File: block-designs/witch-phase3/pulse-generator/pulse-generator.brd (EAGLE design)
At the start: 159.8 x 99.1 mm, 104 parts, among them IC1 74LVC1G17DBV, IC10 74LVC1G08DBV, IC11 74LVC1G08DBV, IC12 741G175, IC13 741G175, IC14 741G175, IC15 741G175, IC16 741G175, IC17 74LVC1G04DBV, IC18 74LVC1G04DBV, IC19 74LVC1G08DBV, IC2 74LVC1G17DBV, IC20 74LVC1G04DBV, IC21 74LVC1G08DBV, IC22 741G175, IC23 74LVC1G08DBV, IC24 74LVC1G04DBV, IC3 74LVC1G17DBV, IC4 NE555D, IC5 741G175, IC6 74LVC1G04DBV, IC7 74LVC1G04DBV, IC8 741G175, IC9 741G175, J1 POWER_JACKPTH, Q1 MMBT2222A, Q2 MMBT2222A, Q3 MMBT2222A, Q4 MMBT2222A, Q5 MMBT2222A, Q6 MMBT2907ALT1SMD, Q7 MMBT2222A, Q8 MMBT2222A, Q9 MMBT2222A

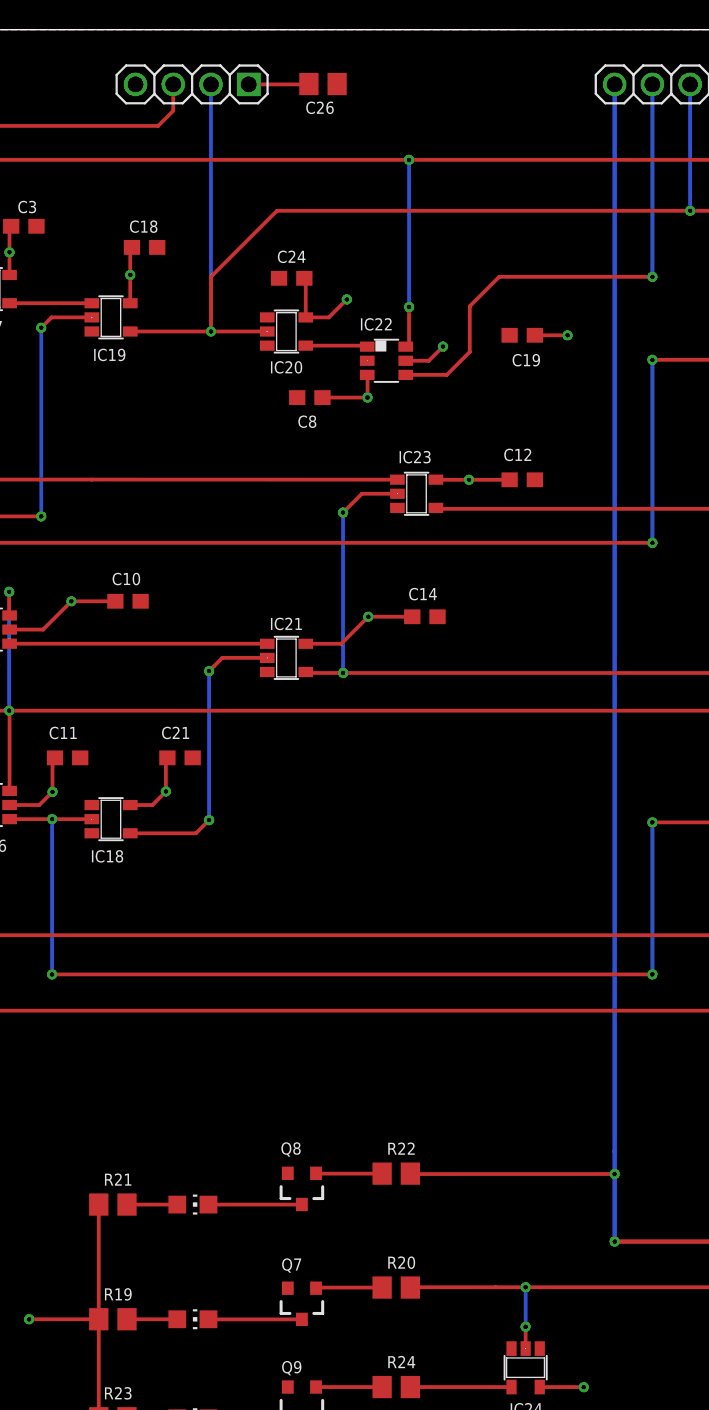
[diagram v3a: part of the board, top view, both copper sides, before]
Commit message: tweak position of function leds
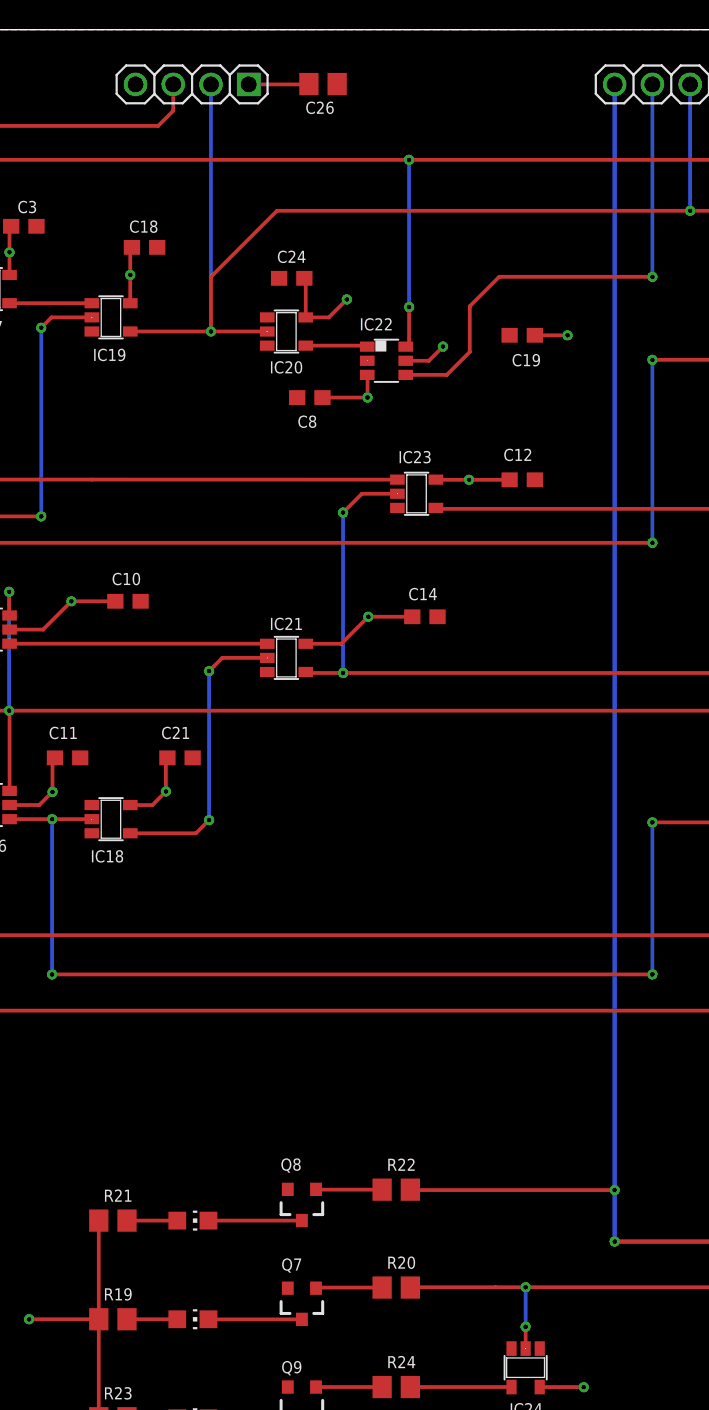
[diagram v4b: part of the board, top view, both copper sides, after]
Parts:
- moved LED8 1.08 mm to (85.6, 18.9)
- moved R21 1.08 mm to (80.3, 18.9)
- moved Q8 1.08 mm to (93.0, 20.0)
- moved R22 1.08 mm to (99.3, 21.0)
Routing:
- net VCC: track 204.5 -> 203.4 mm
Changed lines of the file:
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@@
 <setting verticaltext="up"/>
 </settings>
-<grid distance="0.001" unitdist="inch" unit="inch" style="lines" multiple="1" display="yes" altdistance="0.025" altunitdist="inch" altunit="inch"/>
+<grid distance="0.0005" unitdist="inch" unit="inch" style="lines" multiple="1" display="yes" altdistance="0.025" altunitdist="inch" altunit="inch"/>
 <layers>
 <layer number="1" name="Top" color="4" fill="1" visible="yes" active="yes"/>
@@
 <text x="147.193" y="41.656" size="1.778" layer="48" align="center">CDONE</text>
 <text x="6.35" y="78.3336" size="0.8128" layer="48">Revision 3</text>
-<text x="85.6488" y="22.0472" size="1.778" layer="48" align="center">CLR</text>
+<text x="85.6488" y="20.9677" size="1.778" layer="48" align="center">CLR</text>
 <text x="85.6488" y="14.3256" size="1.778" layer="48" align="center">SUB</text>
 <text x="85.6488" y="7.8486" size="1.778" layer="48" align="center">ADD</text>
@@
 <attribute name="VALUE" x="94.0054" y="13.5255" size="0.4064" layer="27" rot="R180"/>
 </element>
-<element name="LED8" library="led" package="CHIP-LED0805" value="" x="85.6488" y="19.9644" smashed="yes" rot="R270">
-<attribute name="VALUE" x="84.3788" y="17.4244" size="1.27" layer="27"/>
-</element>
-<element name="R21" library="resistor" package="R0805" value="270" x="80.264" y="19.9644" smashed="yes">
-<attribute name="NAME" x="79.629" y="21.2344" size="0.8128" layer="25"/>
-<attribute name="VALUE" x="79.629" y="17.4244" size="1.27" layer="27"/>
-</element>
-<element name="R22" library="resistor" package="R0805" value="1K" x="99.3394" y="22.0472" smashed="yes">
-<attribute name="NAME" x="98.7044" y="23.3172" size="0.8128" layer="25"/>
-<attribute name="VALUE" x="98.7044" y="19.5072" size="1.27" layer="27"/>
-</element>
-<element name="Q8" library="SparkFun-DiscreteSemi" package="SOT23-3" value="MMBT2222A" x="92.9894" y="21.0693" smashed="yes" rot="R180">
-<attribute name="PROD_ID" value="TRANS-08049" x="102.0318" y="17.1577" size="1.778" layer="27" rot="R180" display="off"/>
-<attribute name="NAME" x="92.9767" y="24.1427" size="0.8128" layer="25" rot="R180"/>
-<attribute name="VALUE" x="94.0054" y="21.2598" size="0.4064" layer="27" rot="R180"/>
+<element name="LED8" library="led" package="CHIP-LED0805" value="" x="85.6488" y="18.8849" smashed="yes" rot="R270">
+<attribute name="VALUE" x="84.3788" y="16.3449" size="1.27" layer="27"/>
+</element>
+<element name="R21" library="resistor" package="R0805" value="270" x="80.264" y="18.8849" smashed="yes">
+<attribute name="NAME" x="79.629" y="20.1549" size="0.8128" layer="25"/>
+<attribute name="VALUE" x="79.629" y="16.3449" size="1.27" layer="27"/>
+</element>
+<element name="R22" library="resistor" package="R0805" value="1K" x="99.3394" y="20.9677" smashed="yes">
+<attribute name="NAME" x="98.7044" y="22.2377" size="0.8128" layer="25"/>
+<attribute name="VALUE" x="98.7044" y="18.4277" size="1.27" layer="27"/>
+</element>
+<element name="Q8" library="SparkFun-DiscreteSemi" package="SOT23-3" value="MMBT2222A" x="92.9894" y="19.9898" smashed="yes" rot="R180">
+<attribute name="PROD_ID" value="TRANS-08049" x="102.0318" y="16.0782" size="1.778" layer="27" rot="R180" display="off"/>
+<attribute name="NAME" x="92.9767" y="23.0632" size="0.8128" layer="25" rot="R180"/>
+<attribute name="VALUE" x="94.0054" y="20.1803" size="0.4064" layer="27" rot="R180"/>
 </element>
 <element name="LED9" library="led" package="CHIP-LED0805" value="" x="85.6488" y="5.5802" smashed="yes" rot="R270">
@@
 <contactref element="IC24" pad="5"/>
 <wire x1="79.314" y1="5.5802" x2="79.314" y2="12.2428" width="0.254" layer="1"/>
-<wire x1="79.314" y1="12.2428" x2="79.314" y2="19.9644" width="0.254" layer="1"/>
+<wire x1="79.314" y1="12.2428" x2="79.314" y2="18.8849" width="0.254" layer="1"/>
 <wire x1="79.314" y1="12.2428" x2="74.6252" y2="12.2428" width="0.254" layer="1"/>
 <via x="74.6252" y="12.2428" extent="1-16" drill="0.3048"/>
@@
 <contactref element="IC2" pad="4"/>
 <contactref element="JP3" pad="11"/>
-<wire x1="114.046" y1="95.377" x2="114.046" y2="23.5204" width="0.3048" layer="16"/>
+<wire x1="114.046" y1="95.377" x2="114.046" y2="20.9398" width="0.3048" layer="16"/>
 <via x="114.046" y="17.4727" extent="1-16" drill="0.3048"/>
-<wire x1="114.046" y1="23.5204" x2="114.046" y2="22.0218" width="0.3048" layer="16"/>
-<wire x1="114.046" y1="22.0218" x2="114.046" y2="17.4727" width="0.3048" layer="16"/>
+<wire x1="114.046" y1="20.9398" x2="114.046" y2="17.4727" width="0.3048" layer="16"/>
 <wire x1="114.046" y1="17.4727" x2="129.51" y2="17.4727" width="0.3048" layer="1"/>
 <contactref element="R22" pad="2"/>
-<wire x1="100.3173" y1="22.0193" x2="100.2894" y2="22.0472" width="0.254" layer="1"/>
-<wire x1="100.3173" y1="22.0193" x2="114.046" y2="22.0218" width="0.254" layer="1"/>
-<via x="114.046" y="22.0218" extent="1-16" drill="0.3048"/>
+<wire x1="100.3173" y1="20.9398" x2="100.2894" y2="20.9677" width="0.254" layer="1"/>
+<wire x1="100.3173" y1="20.9398" x2="114.046" y2="20.9398" width="0.254" layer="1"/>
+<via x="114.046" y="20.9398" extent="1-16" drill="0.3048"/>
 </signal>
 <signal name="CARRY_DONE">
@@
 <contactref element="Q8" pad="3"/>
 <contactref element="LED8" pad="C"/>
-<wire x1="86.6988" y1="19.9644" x2="92.9845" y2="19.9644" width="0.254" layer="1"/>
-<wire x1="92.9845" y1="19.9644" x2="92.9894" y2="19.9693" width="0.254" layer="1"/>
+<wire x1="86.6988" y1="18.8849" x2="92.9845" y2="18.8849" width="0.254" layer="1"/>
+<wire x1="92.9845" y1="18.8849" x2="92.9894" y2="18.8898" width="0.254" layer="1"/>
 </signal>
 <signal name="N$22">
 <contactref element="Q8" pad="1"/>
 <contactref element="R22" pad="1"/>
-<wire x1="98.3894" y1="22.0472" x2="93.9488" y2="22.0472" width="0.254" layer="1"/>
-<wire x1="93.9488" y1="22.0472" x2="93.9394" y2="22.0693" width="0.254" layer="1"/>
+<wire x1="98.3894" y1="20.9677" x2="93.9488" y2="20.9677" width="0.254" layer="1"/>
+<wire x1="93.9488" y1="20.9677" x2="93.9394" y2="20.9898" width="0.254" layer="1"/>
 </signal>
 <signal name="N$27">
 <contactref element="LED8" pad="A"/>
 <contactref element="R21" pad="2"/>
-<wire x1="84.5988" y1="19.9644" x2="81.214" y2="19.9644" width="0.254" layer="1"/>
+<wire x1="84.5988" y1="18.8849" x2="81.214" y2="18.8849" width="0.254" layer="1"/>
 </signal>
 <signal name="N$29">
